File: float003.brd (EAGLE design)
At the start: 34.5 x 34 mm, 34 parts, among them X2 USB-MICROB, Y1 16MHz

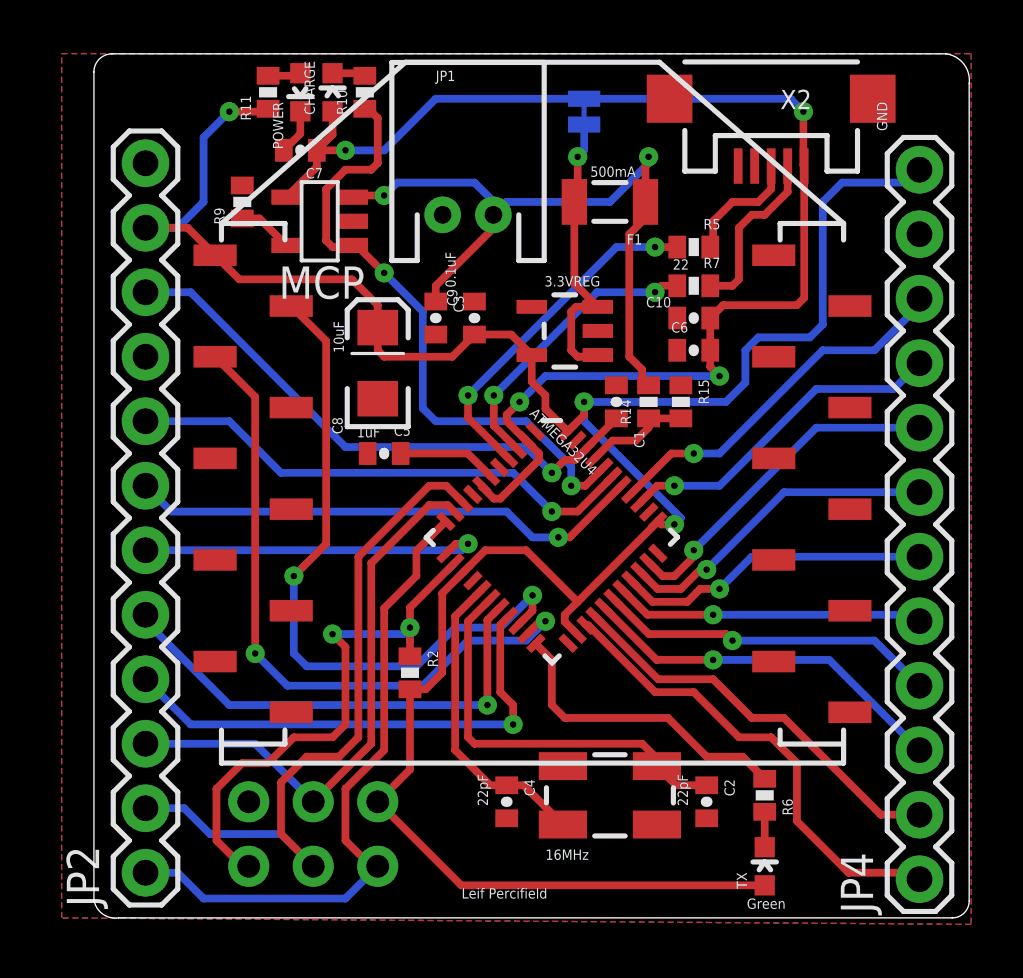
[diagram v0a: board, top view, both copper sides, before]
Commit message: added switch and microsd card
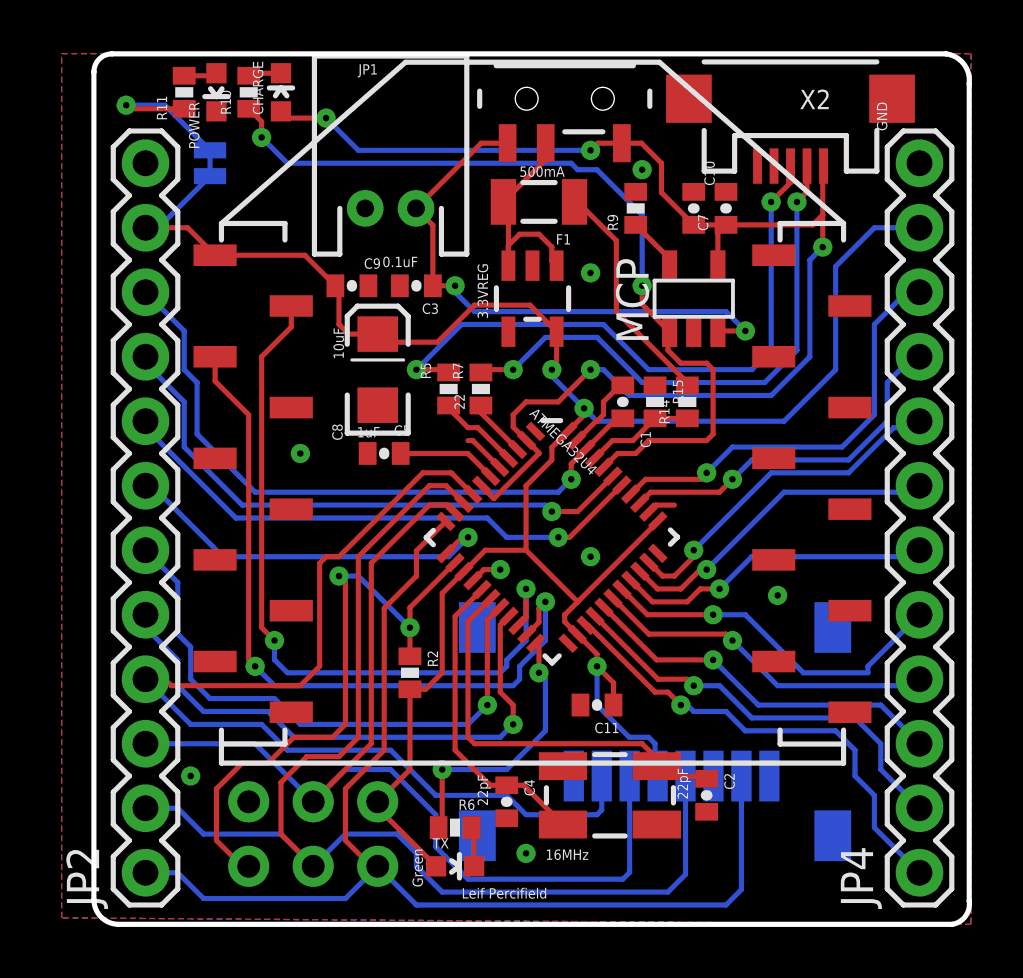
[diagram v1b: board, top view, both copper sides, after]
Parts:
- removed C6: 1uF, SparkFun:0402-CAP
- removed SJ2: USB Power, SparkFun:SJ_2S-TRACE
- added C11: 100nF, SparkFun-Passives:0402-CAP
- added SJ1: Power LED, SparkFun:SJ_2S-TRACE
- added TF1: FLIP_TF, Holders:FLIP_TF
- added U$1: SWITCH-SPDT-A, SparkFun-Electromechanical:SWITCH-SPDT-A
- moved C7 16.9 mm to (63.8, 60.7), turned to 90 degrees
- moved R9 15.5 mm to (60.2, 60.7)
- moved MCP 15.0 mm to (62.5, 57.1), turned to 0 degrees
- moved R6 12.3 mm to (53.1, 36.3), turned to 0 degrees
- moved TX 12.2 mm to (53.1, 34.8), turned to 270 degrees
- moved R5 11.2 mm to (52.8, 53.6), turned to 90 degrees
- moved R7 9.32 mm to (54.1, 53.6), turned to 90 degrees
- moved C9 4.99 mm to (49.0, 57.7), turned to 180 degrees
- moved R10 4.57 mm to (45.0, 65.3)
- moved C10 4.32 mm to (62.5, 60.7), turned to 90 degrees
- moved POWER 3.30 mm to (43.7, 65.3)
- moved R11 3.30 mm to (42.4, 65.3)
- moved JP1 3.06 mm to (50.5, 60.7)
- moved F1 2.79 mm to (56.4, 61.0)
- moved CHARGE 2.03 mm to (46.2, 65.3)
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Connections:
- new net N$22: R11.2, SJ1.1
- new net VBATT_RAW: C3.1, JP1.2, MCP.3, U$1.3
- net +3V3: now also C11.1, JP4.11, SJ1.2, TF1.4; no longer JP4.12, R11.2
- net A2: now also JP2.8; no longer JP2.7
- net A3: now also JP2.9; no longer JP2.8
- net D11: now also JP2.7; no longer JP2.6
- net D14: now also JP2.4, TF1.2
- net D2: now also JP2.5; no longer JP2.4
- net D3: now also JP2.6; no longer JP2.5
- net GND: now also C11.2, JP4.12, TF1.6, TF1.GND@1, TF1.GND@2, TF1.GND@3, TF1.GND@4; no longer C6.1, JP4.11
- net MISO: now also TF1.7
- net MOSI: now also TF1.3
- net RAW: now also U$1.2; no longer SJ2.1
- net SCK: now also TF1.5
- net UVCC: now also U$1.1; no longer C6.2, SJ2.2
- net VBATT: no longer C3.1, JP1.2, MCP.3
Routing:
- net D14: track 0.00 -> 40.8 mm
- net VBATT_RAW: track 0.00 -> 22.3 mm, vias 0 -> 2
- net SCK: track 27.9 -> 48.5 mm
- net N$8: track 4.78 -> 24.6 mm, vias 0 -> 2
- net MISO: track 26.0 -> 45.7 mm
- net MOSI: track 22.3 -> 41.7 mm
- net VBATT: track 27.8 -> 9.14 mm, vias 2 -> 0
- net N$6: track 6.79 -> 21.7 mm, vias 0 -> 2
- net +3V3: track 99.4 -> 87.7 mm
- net D+: track 13.8 -> 3.29 mm, vias 2 -> 0
- net D-: track 11.5 -> 2.33 mm, vias 2 -> 0
- net CHARGE_STAT: track 24.9 -> 32.9 mm
- net N$22: track 0.00 -> 6.38 mm, vias 0 -> 1
- net GND: track 1.81 -> 7.07 mm, vias 0 -> 8
- net D3: track 19.1 -> 22.6 mm
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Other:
- board size 34.5 x 34 mm -> 34.5 x 34.3 mm
